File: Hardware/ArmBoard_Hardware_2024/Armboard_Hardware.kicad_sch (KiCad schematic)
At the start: 110 parts, among them J1 RJ45_LED_Shielded, Q1 BSS138, SW1 SW_SPDT, SW10 SW_Push, SW11 SW_Push, SW2 SW_Push, SW3 SW_Push, SW4 SW_Push, SW5 SW_Push, SW6 SW_Push, SW7 SW_Push, SW8 SW_Push, SW9 SW_Push, U1 OKI, U2 Teensy4.1_DEV-16771, U3 74LS148, U4 74LS148, U5 74HC00, U6 OKI

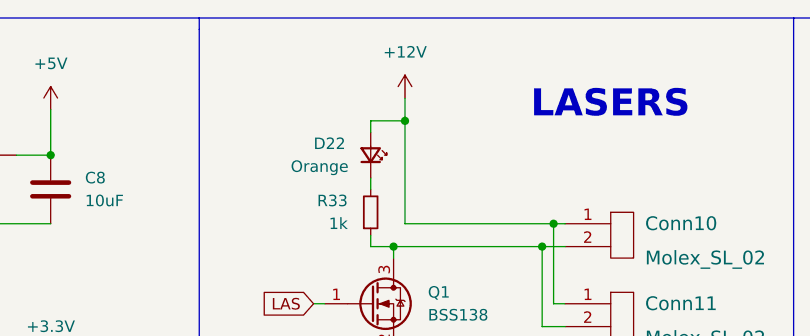
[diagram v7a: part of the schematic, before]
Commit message: label changes
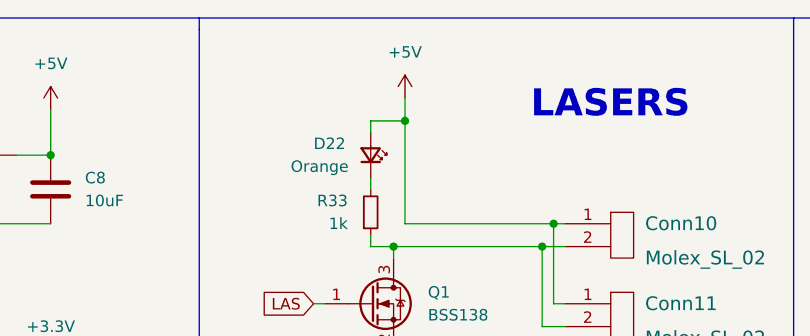
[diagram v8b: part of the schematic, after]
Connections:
- net +12V: no longer Conn10.1, Conn11.1, D22.2 (A)
- net +5V: now also Conn10.1, Conn11.1, D22.2 (A)
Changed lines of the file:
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@@
+    )
+  )
+  (symbol (lib_name "+5V_3") (lib_id "power:+5V") (at 158.75 21.59 0) (unit 1)
+    (in_bom yes) (on_board yes) (dnp no) (fields_autoplaced)
+    (property "Reference" "#PWR063" (at 158.75 25.4 0)
+      (effects (font (size 1.27 1.27)) hide)
+    )
+    (property "Value" "+5V" (at 158.75 16.51 0)
+      (effects (font (size 1.27 1.27)))
+    )
+    (property "Footprint" "" (at 158.75 21.59 0)
+      (effects (font (size 1.27 1.27)) hide)
+    )
+    (property "Datasheet" "" (at 158.75 21.59 0)
+      (effects (font (size 1.27 1.27)) hide)
+    )
+    (pin "1")
+    (instances
+      (project "Armboard_Hardware"
+        (path "/0313b944-1194-481e-8200-b9ebb32d70a5"
+          (reference "#PWR063") (unit 1)
+        )
+      )
     )
   )
@@
         )
       )
-    )
-  )
-  (symbol (lib_id "power:+12V") (at 158.75 21.59 0) (unit 1)
-    (in_bom yes) (on_board yes) (dnp no) (fields_autoplaced)
-    (property "Reference" "#PWR063" (at 158.75 25.4 0)
-      (effects (font (size 1.27 1.27)) hide)
-    )
-    (property "Value" "+12V" (at 158.75 16.51 0)
-      (effects (font (size 1.27 1.27)))
-    )
-    (property "Footprint" "" (at 158.75 21.59 0)
-      (effects (font (size 1.27 1.27)) hide)
-    )
-    (property "Datasheet" "" (at 158.75 21.59 0)
-      (effects (font (size 1.27 1.27)) hide)
-    )
-    (pin "1")
-    (instances
-      (project "Armboard_Hardware"
-        (path "/0313b944-1194-481e-8200-b9ebb32d70a5"
-          (reference "#PWR063") (unit 1)
-        )
-      )
-      (project "Armboard_Hardware"
-        (path "/bac7748c-30df-4d2c-bf90-90bc7b9f8a10"
-          (reference "#PWR0104") (unit 1)
-        )
-      )
